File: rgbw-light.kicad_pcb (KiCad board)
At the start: 2 copper layers, 36 x 36 mm, 25 parts, among them CN1 1x8, CN2 1x8, IC1 PAM2804AAB010, IC2 PAM2804AAB010, IC3 PAM2804AAB010, IC4 PAM2804AAB010

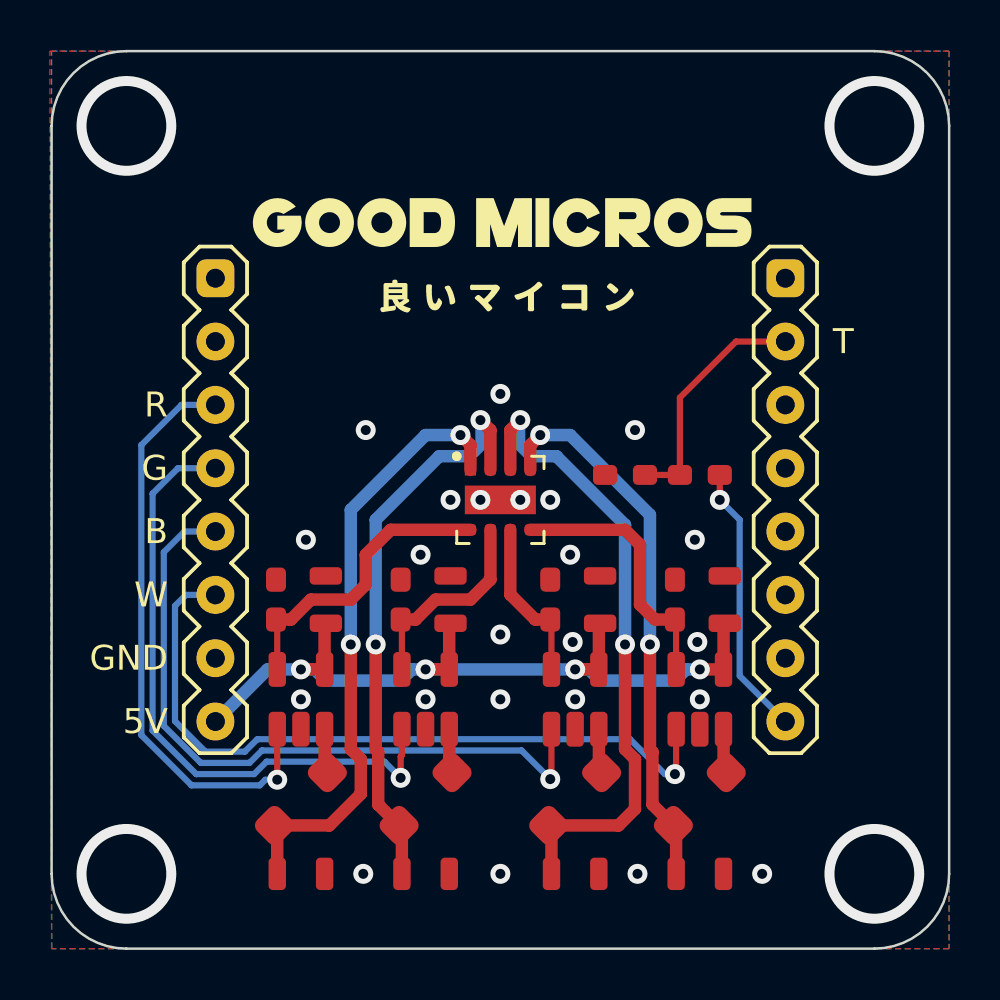
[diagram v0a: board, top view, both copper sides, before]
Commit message: moved blue from FLASH pin to GPIO12
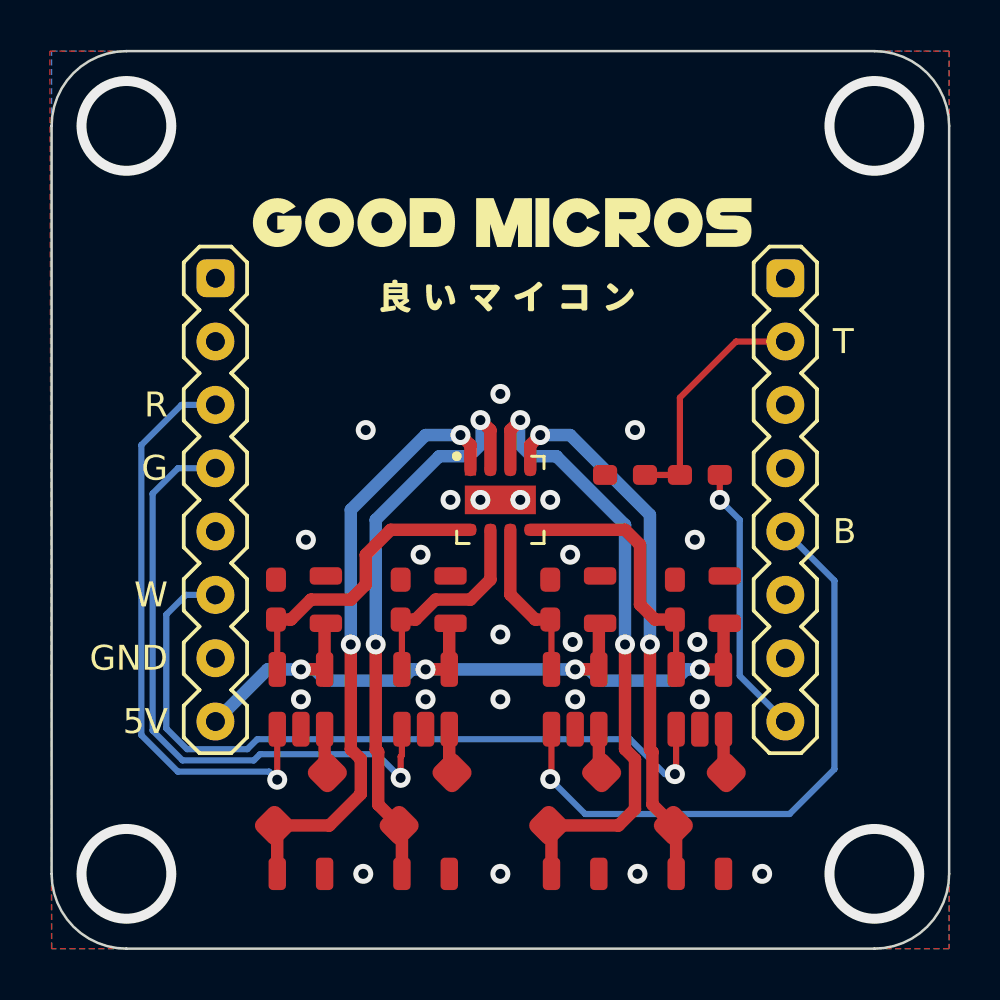
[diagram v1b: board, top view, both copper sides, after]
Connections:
- CN1 pad 5: /B -> unconnected-(CN1-Pad5)
- CN2 pad 5: unconnected-(CN2-Pad5) -> /B
- D1 pad 0: GND -> (no net)
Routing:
- net /B: track 28.2 -> 25.1 mm
- net /W: track 29.6 -> 30.2 mm
